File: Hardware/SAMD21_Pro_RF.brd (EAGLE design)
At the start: 44.5 x 30.5 mm, 130 parts, among them J12 JST, J13 U.FL, J7 PTH, J9 External On/Off, Q1 2.5A/30V, U1 MCP73831, U3 RFM95W, U4 ATSAMD21G, U6 3.3V, Y1 32.768kHz

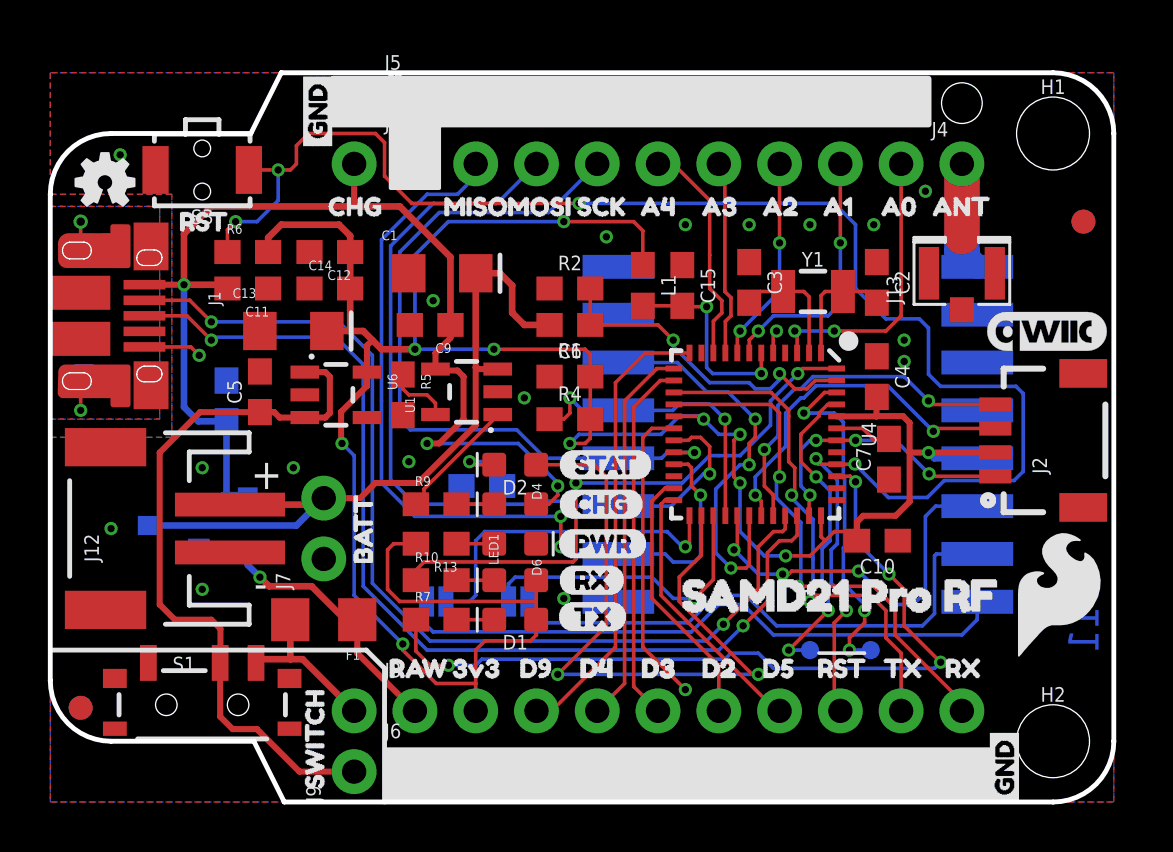
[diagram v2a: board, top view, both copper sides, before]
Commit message: included PTH headers for SWD lines
note, I did not move test points.
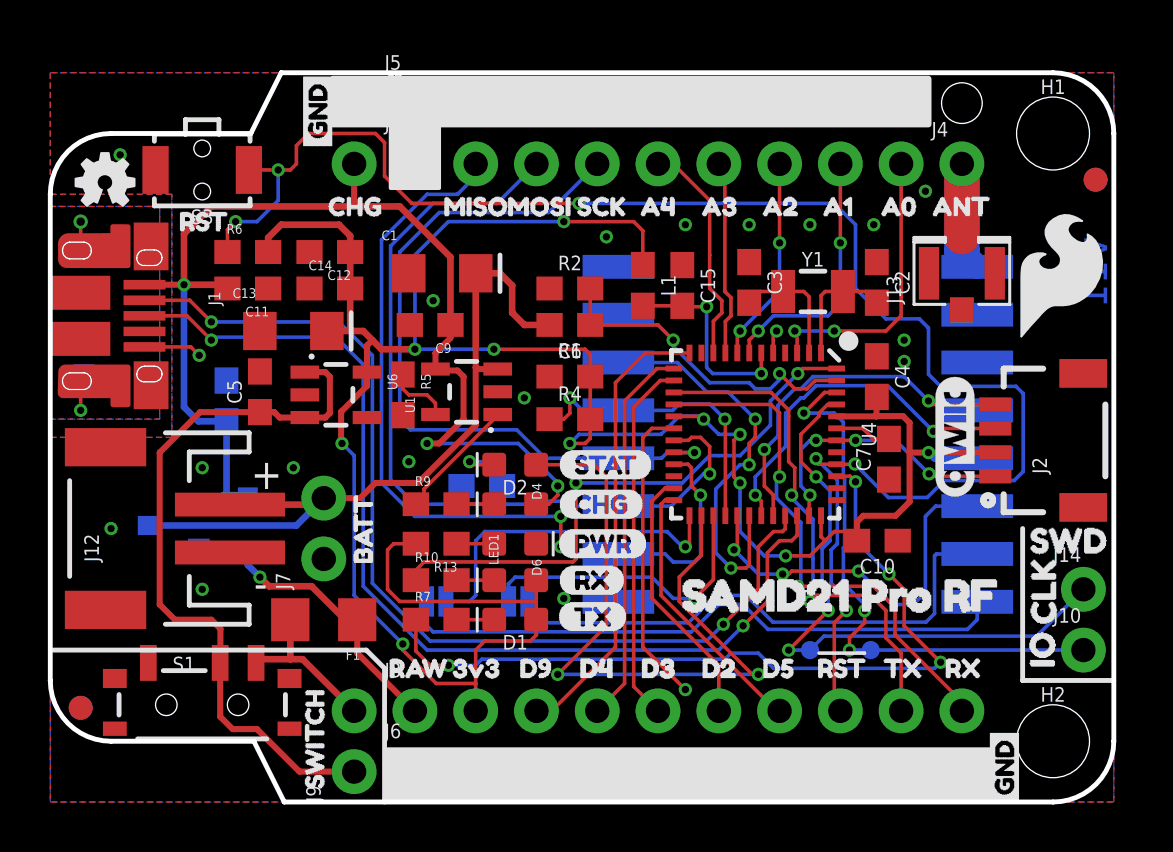
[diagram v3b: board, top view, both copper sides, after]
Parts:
- added J10, J14: (no value), SparkFun-Connectors:1X01_NO_SILK
- added U$34, U$64: (no value), buzzard_labels (1):IO3
- added U$56, U$60: (no value), buzzard_labels (1):CLK4
- added U$58, U$59: (no value), buzzard_labels (1):SWD2
- moved U$51 13.3 mm to (40.2, 19.2)
- moved LOGO3 5.87 mm to (37.8, 15.2), turned to 90 degrees
- moved FD2 1.82 mm to (43.7, 26.0)
- moved FD4 1.82 mm to (43.7, 26.0)
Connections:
- net SWDCLK: now also J14.1
- net SWDIO: now also J10.1
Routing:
- net SWDCLK: track 13.4 -> 25.9 mm
- net SWDIO: track 14.6 -> 23.5 mm
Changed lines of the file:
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@@
 <vertex x="36.703" y="28.321"/>
 </polygon>
-<text x="43.815" y="9.144" size="1.27" layer="16" font="vector" ratio="15" rot="SMR270">v11</text>
+<text x="44.1706" y="23.622" size="1.27" layer="16" font="vector" ratio="15" rot="SMR270">v11</text>
 <wire x1="13.97" y1="0" x2="13.97" y2="5.588" width="0.2032" layer="22"/>
 <wire x1="13.97" y1="5.588" x2="13.208" y2="6.35" width="0.2032" layer="22"/>
@@
 <text x="15.24" y="-15.24" size="1.778" layer="51" font="vector" ratio="12">Pete Lewis</text>
 <text x="-2.54" y="-15.24" size="1.778" layer="51" font="vector" ratio="12">Revised by:</text>
+<wire x1="40.64" y1="11.43" x2="40.64" y2="5.08" width="0.2032" layer="21"/>
+<wire x1="40.64" y1="5.08" x2="44.45" y2="5.08" width="0.2032" layer="21"/>
+<wire x1="40.64" y1="11.43" x2="40.64" y2="5.08" width="0.2032" layer="22"/>
+<wire x1="44.45" y1="5.08" x2="40.64" y2="5.08" width="0.2032" layer="22"/>
 </plain>
 <attributes>
@@
 </element>
 <element name="FD1" library="SparkFun-Aesthetics" package="FIDUCIAL-1X2" value="FIDUCIAL1X2" x="1.27" y="3.937" smashed="yes" rot="MR0"/>
-<element name="FD2" library="SparkFun-Aesthetics" package="FIDUCIAL-1X2" value="FIDUCIAL1X2" x="43.18" y="24.257" smashed="yes" rot="MR0"/>
+<element name="FD2" library="SparkFun-Aesthetics" package="FIDUCIAL-1X2" value="FIDUCIAL1X2" x="43.688" y="26.0096" smashed="yes" rot="MR0"/>
 <element name="FD3" library="SparkFun-Aesthetics" package="FIDUCIAL-1X2" value="FIDUCIAL1X2" x="1.27" y="3.937" smashed="yes"/>
-<element name="FD4" library="SparkFun-Aesthetics" package="FIDUCIAL-1X2" value="FIDUCIAL1X2" x="43.18" y="24.257" smashed="yes"/>
+<element name="FD4" library="SparkFun-Aesthetics" package="FIDUCIAL-1X2" value="FIDUCIAL1X2" x="43.688" y="26.0096" smashed="yes"/>
 <element name="Y1" library="SparkFun-Clocks" package="CRYSTAL-SMD-3.2X1.5MM" value="32.768kHz" x="31.877" y="21.336" smashed="yes">
 <attribute name="NAME" x="31.877" y="22.379" size="0.6096" layer="25" font="vector" ratio="20" align="bottom-center"/>
@@
 <attribute name="VALUE" x="41.91" y="0.889" size="0.6096" layer="27" font="vector" ratio="20" align="top-center"/>
 </element>
-<element name="U$51" library="SparkFun-Aesthetics" package="SFE_LOGO_FLAME_.2" value="" x="40.132" y="5.842" smashed="yes"/>
+<element name="U$51" library="SparkFun-Aesthetics" package="SFE_LOGO_FLAME_.2" value="" x="40.2336" y="19.177" smashed="yes"/>
 <element name="D3" library="SparkFun-DiscreteSemi" package="SOD-323" value="1A/23V/620mV" x="8.255" y="11.684" smashed="yes" rot="MR90">
 <attribute name="NAME" x="9.017" y="11.684" size="0.6096" layer="26" font="vector" ratio="20" rot="MR90" align="bottom-center"/>
@@
 <attribute name="VALUE" x="35.814" y="14.3256" size="0.6096" layer="27" font="vector" ratio="20" rot="R90" align="top-center"/>
 </element>
-<element name="LOGO3" library="SparkFun-Aesthetics" package="QWIIC_5MM" value="QWIIC_LOGO_5MM" x="41.6306" y="19.685" smashed="yes"/>
+<element name="LOGO3" library="SparkFun-Aesthetics" package="QWIIC_5MM" value="QWIIC_LOGO_5MM" x="37.7952" y="15.24" smashed="yes" rot="R90"/>
+<element name="J10" library="SparkFun-Connectors" package="1X01_NO_SILK" value="" x="43.18" y="6.35" smashed="yes">
+<attribute name="NAME" x="41.91" y="7.493" size="0.6096" layer="25" font="vector" ratio="20"/>
+<attribute name="VALUE" x="41.91" y="4.572" size="0.6096" layer="27" font="vector" ratio="20"/>
+</element>
+<element name="J14" library="SparkFun-Connectors" package="1X01_NO_SILK" value="" x="43.18" y="8.89" smashed="yes">
+<attribute name="NAME" x="41.91" y="10.033" size="0.6096" layer="25" font="vector" ratio="20"/>
+<attribute name="VALUE" x="41.91" y="7.112" size="0.6096" layer="27" font="vector" ratio="20"/>
+</element>
+<element name="U$34" library="buzzard_labels (1)" package="IO3" value="" x="41.4528" y="4.699" smashed="yes" rot="R90"/>
+<element name="U$56" library="buzzard_labels (1)" package="CLK4" value="" x="41.5036" y="6.5278" smashed="yes" rot="R90"/>
+<element name="U$58" library="buzzard_labels (1)" package="SWD2" value="" x="40.005" y="10.922" smashed="yes"/>
+<element name="U$59" library="buzzard_labels (1)" package="SWD2" value="" x="45.0596" y="10.922" smashed="yes" rot="MR0"/>
+<element name="U$60" library="buzzard_labels (1)" package="CLK4" value="" x="41.5036" y="6.5024" smashed="yes" rot="MR90"/>
+<element name="U$64" library="buzzard_labels (1)" package="IO3" value="" x="41.4782" y="4.699" smashed="yes" rot="MR90"/>
 </elements>
 <signals>
@@
 <wire x1="34.036" y1="8.255" x2="33.147" y2="9.144" width="0.1524" layer="16"/>
 <wire x1="32.766" y1="16.256" x2="33.147" y2="15.875" width="0.1524" layer="16"/>
+<contactref element="J10" pad="1"/>
+<wire x1="34.29" y1="6.35" x2="43.18" y2="6.35" width="0.1524" layer="16"/>
 </signal>
 <signal name="SWDCLK">
@@
 <wire x1="32.512" y1="8.001" x2="30.861" y2="6.35" width="0.1524" layer="1"/>
 <wire x1="30.861" y1="6.35" x2="31.75" y2="6.35" width="0.1524" layer="16"/>
+<contactref element="J14" pad="1"/>
+<wire x1="31.75" y1="6.35" x2="32.3342" y2="6.9342" width="0.1524" layer="16"/>
+<wire x1="41.2242" y1="6.9342" x2="43.18" y2="8.89" width="0.1524" layer="16"/>
+<wire x1="32.3342" y1="6.9342" x2="41.2242" y2="6.9342" width="0.1524" layer="16"/>
 </signal>
 <signal name="MOSI">
@@
 <contactref element="U3" pad="DIO1"/>
 <contactref element="JP3" pad="1"/>
-<wire x1="36.957" y1="7.874" x2="36.449" y2="7.366" width="0.1524" layer="16"/>
+<wire x1="36.957" y1="7.874" x2="36.6014" y2="7.5184" width="0.1524" layer="16"/>
 <wire x1="29.083" y1="8.636" x2="27.813" y2="8.636" width="0.1524" layer="16"/>
 <wire x1="26.67" y1="7.493" x2="27.813" y2="8.636" width="0.1524" layer="16"/>
@@
 <wire x1="19.9644" y1="8.382" x2="19.9644" y2="7.7216" width="0.1524" layer="16"/>
 <wire x1="19.9644" y1="7.7216" x2="20.193" y2="7.493" width="0.1524" layer="16"/>
-<wire x1="36.449" y1="7.366" x2="35.56" y2="7.366" width="0.1524" layer="16"/>
-<wire x1="35.56" y1="7.366" x2="30.353" y2="7.366" width="0.1524" layer="16"/>
-<wire x1="30.353" y1="7.366" x2="29.083" y2="8.636" width="0.1524" layer="16"/>
+<wire x1="36.6014" y1="7.5184" x2="30.2006" y2="7.5184" width="0.1524" layer="16"/>
+<wire x1="30.2006" y1="7.5184" x2="29.083" y2="8.636" width="0.1524" layer="16"/>
 </signal>
 <signal name="N$18">
@@
 <wire x1="26.797" y1="7.112" x2="27.94" y2="8.255" width="0.1524" layer="16"/>
 <wire x1="38.742" y1="8.367" x2="38.742" y2="7.627" width="0.1524" layer="16"/>
-<wire x1="38.1" y1="6.985" x2="38.742" y2="7.627" width="0.1524" layer="16"/>
+<wire x1="38.3286" y1="7.2136" x2="38.742" y2="7.627" width="0.1524" layer="16"/>
 <wire x1="16.002" y1="7.112" x2="15.7226" y2="7.3914" width="0.1524" layer="16"/>
 <wire x1="16.002" y1="7.112" x2="26.797" y2="7.112" width="0.1524" layer="16"/>
 <wire x1="15.7226" y1="7.3914" x2="15.7226" y2="8.382" width="0.1524" layer="16"/>
-<wire x1="30.226" y1="6.985" x2="38.1" y2="6.985" width="0.1524" layer="16"/>
-<wire x1="28.956" y1="8.255" x2="30.226" y2="6.985" width="0.1524" layer="16"/>
+<wire x1="29.9974" y1="7.2136" x2="38.3286" y2="7.2136" width="0.1524" layer="16"/>
+<wire x1="28.956" y1="8.255" x2="29.9974" y2="7.2136" width="0.1524" layer="16"/>
 </signal>
 <signal name="V_USB">

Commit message: Added LED disable Jumper NC trace
for easier access to disable Power LED in  low power applications
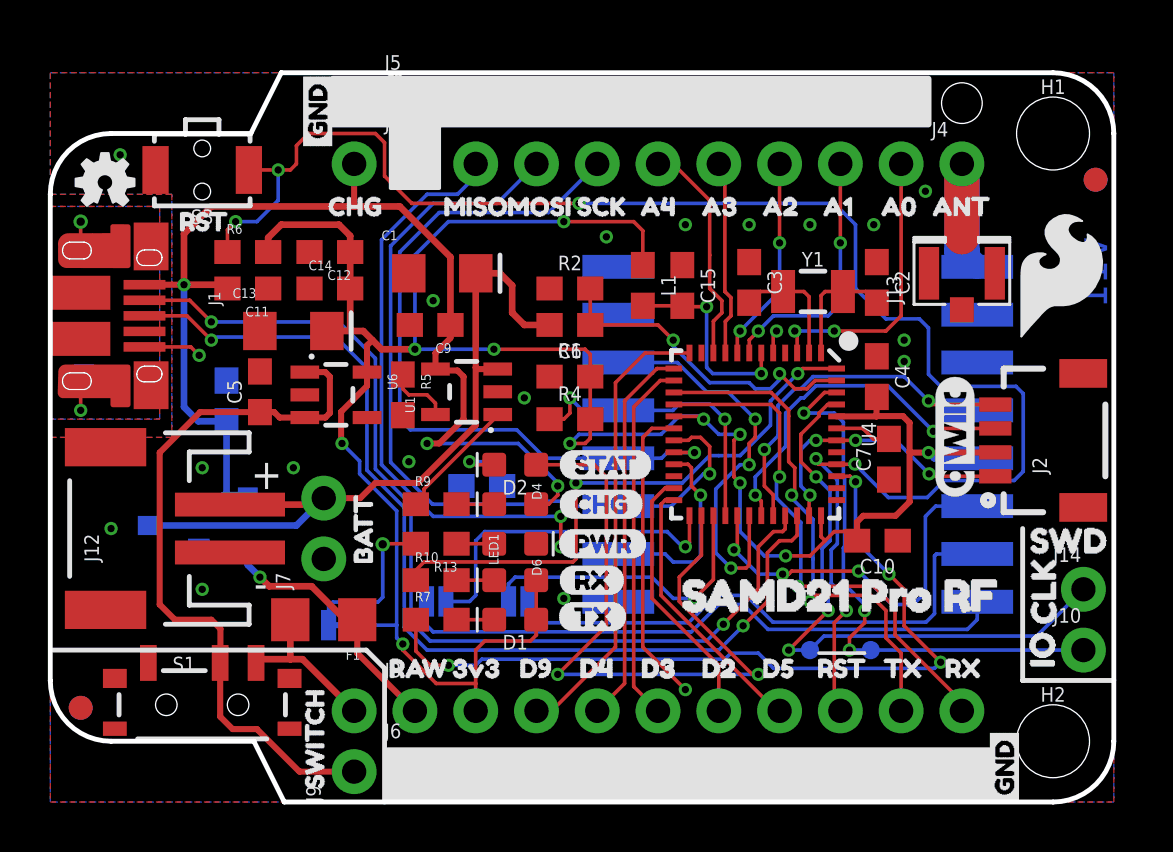
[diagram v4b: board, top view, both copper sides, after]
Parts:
- added LED: (no value), SparkFun-Jumpers:SMT-JUMPER_2_NC_TRACE_SILK
- added U$66: (no value), buzzard_labels (2):LED0
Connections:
- new net N$5: LED.2, R13.2
- net 3.3V: now also LED.1; no longer R13.2
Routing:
- net 3.3V: track 111.9 -> 104.4 mm
- net N$5: track 0.00 -> 6.81 mm, vias 0 -> 1

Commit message: Changed C7 to 1.0uF as recommended in DS
This is the VDDCORE cap to GND.
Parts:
- C7: value 0.1uF -> 1.0uF
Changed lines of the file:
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@@
 <layers>
 <layer number="1" name="Top" color="4" fill="1" visible="yes" active="yes"/>
-<layer number="16" name="Bottom" color="1" fill="1" visible="no" active="yes"/>
+<layer number="16" name="Bottom" color="1" fill="1" visible="yes" active="yes"/>
 <layer number="17" name="Pads" color="2" fill="1" visible="yes" active="yes"/>
 <layer number="18" name="Vias" color="2" fill="1" visible="yes" active="yes"/>
@@
 <attribute name="VALUE" x="9.525" y="17.145" size="0.6096" layer="27" font="vector" ratio="20" rot="R90" align="top-center"/>
 </element>
-<element name="C7" library="SparkFun-Capacitors" package="0603" value="0.1uF" x="35.052" y="14.3256" smashed="yes" rot="R90">
+<element name="C7" library="SparkFun-Capacitors" package="0603" value="1.0uF" x="35.052" y="14.3256" smashed="yes" rot="R90">
 <attribute name="NAME" x="34.29" y="14.3256" size="0.6096" layer="25" font="vector" ratio="20" rot="R90" align="bottom-center"/>
-<attribute name="PROD_ID" value="CAP-00810" x="35.052" y="14.3256" size="1.778" layer="27" font="vector" ratio="15" rot="R90" display="off"/>
-<attribute name="VALUE" x="35.814" y="14.3256" size="0.6096" layer="27" font="vector" ratio="20" rot="R90" align="top-center"/>
+<attribute name="PROD_ID" value="CAP-00868" x="35.052" y="14.3256" size="1.778" layer="27" font="vector" ratio="15" rot="R90" display="off"/>
+<attribute name="VALUE" value="1.0uF" x="35.814" y="14.3256" size="0.6096" layer="27" font="vector" ratio="20" rot="R90" align="top-center"/>
 </element>
 <element name="LOGO3" library="SparkFun-Aesthetics" package="QWIIC_5MM" value="QWIIC_LOGO_5MM" x="37.7952" y="15.24" smashed="yes" rot="R90"/>

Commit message: Adds new panel
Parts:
- moved U$26 108.5 mm to (52.1, 49.5)
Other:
- board text added: "Board Thickness: 0.8mm"
- board text removed: "0.8mm Board Thickness"
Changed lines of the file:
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@@
 <?xml version="1.0" encoding="utf-8"?>
 <!DOCTYPE eagle SYSTEM "eagle.dtd">
-<eagle version="9.5.1">
+<eagle version="9.6.2">
 <drawing>
 <settings>
@@
 <text x="10.287" y="12.065" size="1.27" layer="22" font="vector" ratio="15" rot="MR0">+</text>
 <text x="10.541" y="10.795" size="1.27" layer="22" font="vector" ratio="15" rot="MR270">-</text>
-<text x="-15.24" y="-29.21" size="1.778" layer="51" font="vector" ratio="15" align="center">0.8mm Board Thickness</text>
+<text x="53.34" y="36.83" size="1.778" layer="51" font="vector" ratio="15">Board Thickness: 0.8mm </text>
 <wire x1="0" y1="16.002" x2="0" y2="6.35" width="0.1524" layer="22"/>
 <wire x1="0" y1="6.35" x2="5.08" y2="6.35" width="0.1524" layer="22"/>
@@
 <element name="U$25" library="buzzard_labels (3)" package="LORA0" value="" x="22.352" y="10.287" smashed="yes" rot="MR0"/>
 <element name="U$35" library="buzzard_labels (3)" package="WAN1" value="" x="18.923" y="10.287" smashed="yes" rot="MR0"/>
-<element name="U$26" library="SparkFun-Aesthetics" package="ORDERING_INSTRUCTIONS" value="SPECIAL_INSTRUCTIONS-ORDERING" x="-33.02" y="-17.78" smashed="yes"/>
+<element name="U$26" library="SparkFun-Aesthetics" package="ORDERING_INSTRUCTIONS" value="SPECIAL_INSTRUCTIONS-ORDERING" x="52.07" y="49.53" smashed="yes"/>
 <element name="R4" library="SparkFun-Resistors" package="0603" value="10k" x="21.717" y="16.002" smashed="yes">
 <attribute name="NAME" x="21.717" y="16.764" size="0.6096" layer="25" font="vector" ratio="20" align="bottom-center"/>
